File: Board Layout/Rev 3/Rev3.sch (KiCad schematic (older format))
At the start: 7 parts, among them P1 CONN_01X05, P2 CONN_01X05

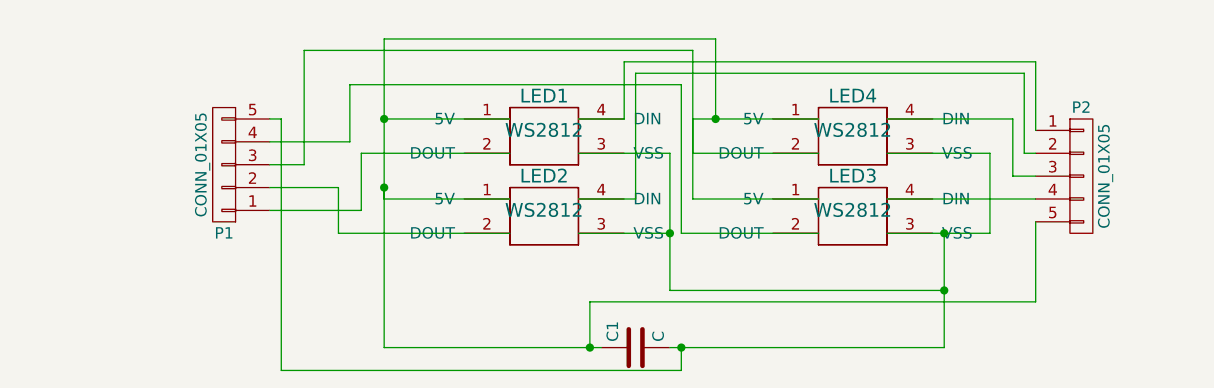
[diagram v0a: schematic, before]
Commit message: New Update
Created a new layout. More condensed. Uses 4 Caps.
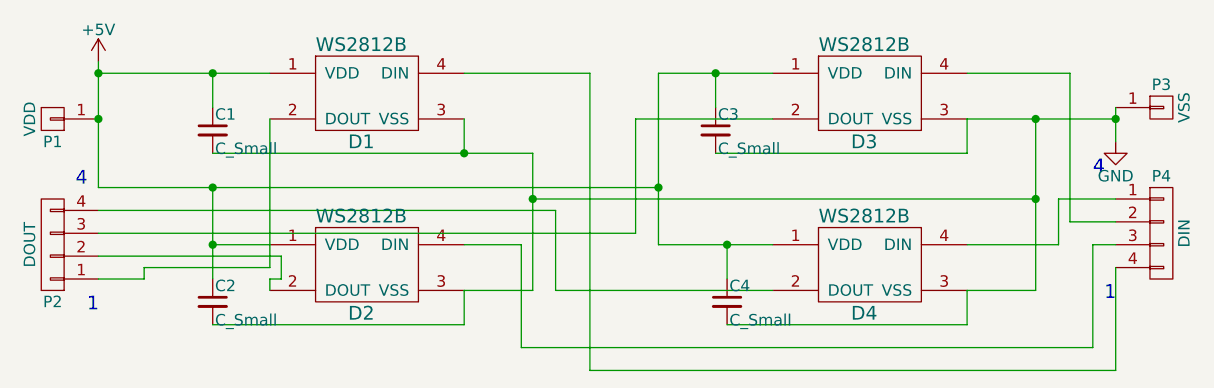
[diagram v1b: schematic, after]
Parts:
- removed C1: C, Capacitors_SMD:C_1206_HandSoldering, symbol C
- removed LED1, LED2, LED3, LED4: WS2812, Rev 3:WS2812B, symbol WS2812
- removed P1, P2: CONN_01X05, Pin_Headers:Pin_Header_Straight_1x05, symbol CONN_01X05
- added C1, C2, C3, C4: C_Small, Capacitors_SMD:C_0603_HandSoldering, symbol C_Small
- added D1, D2, D3, D4: WS2812B, LEDs:LED_WS2812B-PLCC4, symbol WS2812B
- added P1: VDD, Pin_Headers:Pin_Header_Straight_1x01, symbol CONN_01X01
- added P2: DOUT, Pin_Headers:Pin_Header_Straight_1x04, symbol CONN_01X04
- added P3: VSS, Pin_Headers:Pin_Header_Straight_1x01, symbol CONN_01X01
- added P4: DIN, Pin_Headers:Pin_Header_Straight_1x04, symbol CONN_01X04
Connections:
- new net: D1.2 (DOUT), P2.1 (P1)
- new net: D1.4 (DIN), P4.4 (P4)
- new net: D2.2 (DOUT), P2.2 (P2)
- new net: D2.4 (DIN), P4.3 (P3)
- new net: D3.2 (DOUT), P2.3 (P3)
- new net: D3.4 (DIN), P4.2 (P2)
- new net: D4.2 (DOUT), P2.4 (P4)
- new net: D4.4 (DIN), P4.1 (P1)
- new net +5V: C1.1, C2.1, C3.1, C4.1, D1.1 (VDD), D2.1 (VDD), D3.1 (VDD), D4.1 (VDD), P1.1 (P1)
- new net GND: C1.2, C2.2, C3.2, C4.2, D1.3 (VSS), D2.3 (VSS), D3.3 (VSS), D4.3 (VSS), P3.1 (P1)
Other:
- note added: "1"
- note added: "4"
